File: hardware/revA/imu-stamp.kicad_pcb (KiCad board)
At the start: 4 copper layers, 19 x 7.9 mm, 37 parts, among them P1 I/O, P2 I/O, U1 LTC4317, U2 REG710NA-3.3/3K, U3 IAM-20380, U4 MMC5603NJ, U5 MC3419, U6 IAM-20380, U7 MMC5603NJ, U8 MC3419

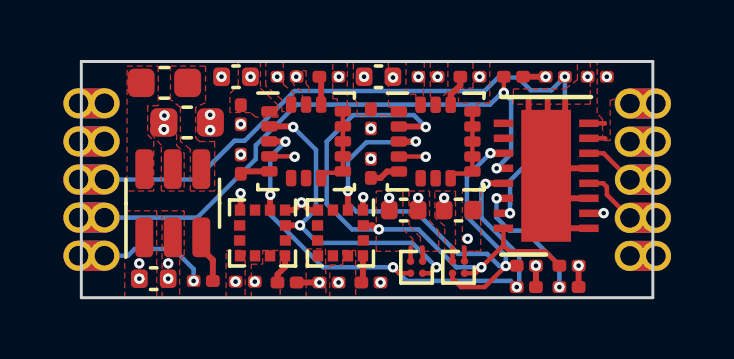
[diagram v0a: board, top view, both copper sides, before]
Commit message: updated iam20380 footprint
to exclude solder mask per AN-IVS-0002A-00
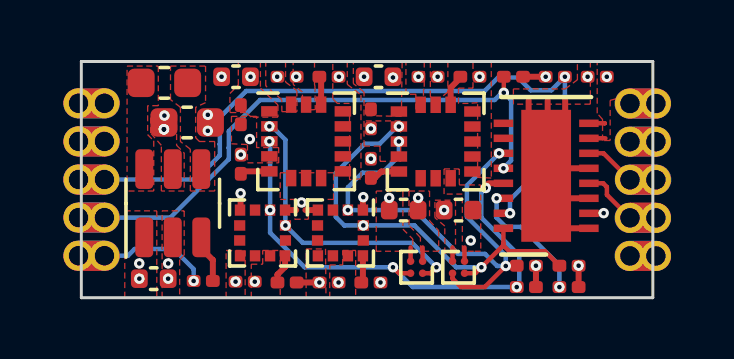
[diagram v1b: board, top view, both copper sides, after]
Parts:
- U3, U6: footprint Package_LGA:LGA-16_3x3mm_P0.5mm_LayoutBorder3x5y -> imu-stamp:IAM-20380
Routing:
- net GND: track 13.8 -> 6.31 mm, vias 22 -> 20
- net /SCL_1: track 17.9 -> 14.2 mm
- net /SDA_1: track 19.1 -> 17.0 mm
- net /SCL_0: track 20.0 -> 19.0 mm
- net /SCL: track 22.4 -> 23.2 mm

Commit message: adjusted castellated hole size and position
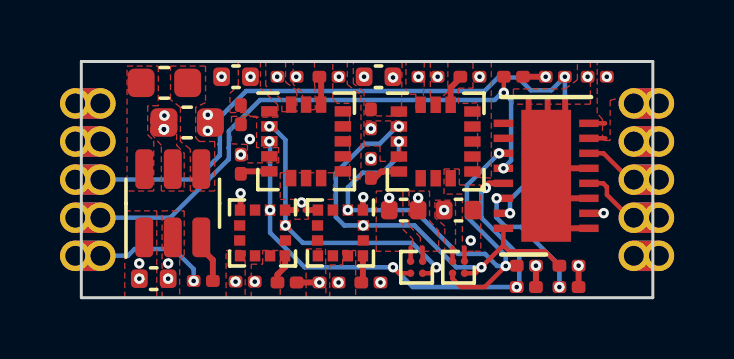
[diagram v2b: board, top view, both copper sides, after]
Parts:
- moved P1 0.14 mm to (115.3, 62.1)
- moved P2 0.13 mm to (133.1, 67.2)

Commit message: consistency updates
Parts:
- removed R1, R5: 10k, Resistor_SMD:R_0201_0603Metric
- added R2: ~, Resistor_SMD:R_0402_1005Metric, B.Cu at (130.8, 66.2)
- added R3: ~, Resistor_SMD:R_0402_1005Metric, B.Cu at (130.8, 64.6)
- added R4: ~, Resistor_SMD:R_0402_1005Metric, B.Cu at (130.8, 63.2)
- U3, U6: footprint imu-stamp:IAM-20380 -> Package_LGA:LGA-16_3x3mm_P0.5mm_LayoutBorder3x5y
- moved C1 0.69 mm to (131.2, 61.2)
- moved U1 0.33 mm to (130.4, 64.3)
- moved C8 0.32 mm to (128.0, 61.2)
- moved C7 0.13 mm to (126.4, 61.2)
- turned R15 to 90 degrees
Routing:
- net GND: track 6.31 -> 29.4 mm, vias 20 -> 22
- net 3.3V: track 5.43 -> 24.3 mm, vias 18 -> 15
- net /SCL_1: track 14.2 -> 19.7 mm
- net /XORL1: track 1.73 -> 6.02 mm
- net /SCL: track 23.2 -> 19.1 mm, vias 2 -> 1
- net /XORL2: track 2.00 -> 5.93 mm
- net Net-(U2-CP+): track 0.00 -> 2.77 mm
- net Net-(U2-CP-): track 0.00 -> 2.54 mm
- net /SCL_0: track 19.0 -> 21.0 mm
- net /SDA: track 18.8 -> 17.2 mm, vias 2 -> 1
- net VCC: track 0.00 -> 1.26 mm, vias 3 -> 2
- net /SDA_1: track 17.0 -> 16.0 mm
- net /SDA_0: track 17.8 -> 18.3 mm
- removed copper zone on F.Cu, net Net-(U2-CP+)
- removed copper zone on F.Cu, net Net-(U2-CP-)
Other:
- board text added: "3V3"
- board text added: "CH 5/23"
- board text removed: "CH 3/23"
- board text removed: "XOR_REF"

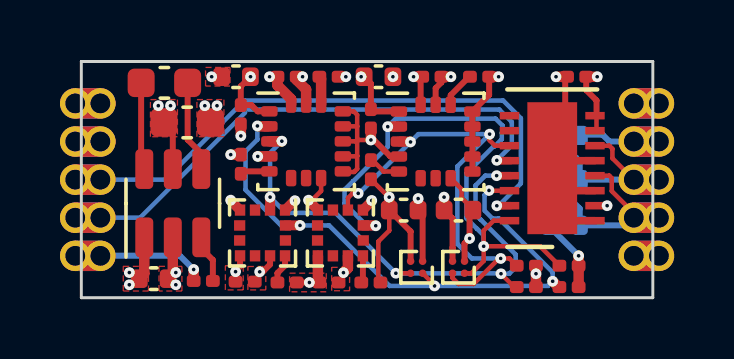
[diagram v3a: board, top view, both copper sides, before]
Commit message: resized board for manufacturing
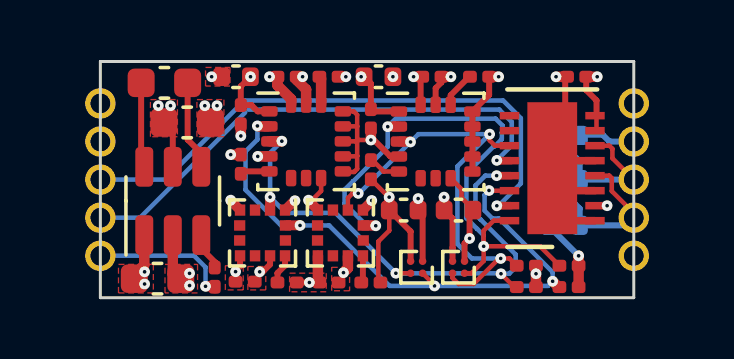
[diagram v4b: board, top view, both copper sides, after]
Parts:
- C4: footprint Capacitor_SMD:C_0402_1005Metric -> Capacitor_SMD:C_0603_1608Metric
- P1, P2: footprint imu-stamp:PinHeaderCastellated_1x05_P1.27mm_Vertical -> imu-stamp:Castellated_1x05_P1.27mm_Vertical
- R11, R12, R13, R14: value 2.7k -> 4.7k
- R2, R3, R4: value ~ -> DNP
- U1: value LTC4317 -> LTC4317I
- moved R9 0.40 mm to (119.1, 67.9), turned to 90 degrees
- moved C4 0.13 mm to (117.2, 67.9)
- moved U2 0.08 mm to (117.7, 65.4)
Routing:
- net /EN: track 3.55 -> 4.92 mm
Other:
- board size 19 x 7.9 mm -> 17.8 x 7.9 mm
- board text added: "0"
- board text added: "0 mm"
- board text added: "0.0091"
- board text added: "0.01 mm"
- board text added: "0.035 mm"
- board text added: "0.1016 mm"
- board text added: "0.11 mm"
- board text added: "0.1270 mm / 0.1270 mm"
- board text added: "0.4 mm"
- board text added: "0.7800 mm"
- board text added: "1"
- board text added: "19.0500 mm x 7.8740 mm"
- board text added: "3.3"
- board text added: "3.69"
- board text added: "4"
- board text added: "B.Cu"
- board text added: "B.Mask"
- board text added: "B.Paste"
- board text added: "B.Silkscreen"
- board text added: "BOARD CHARACTERISTICS"
- board text added: "Board Thickness:"
- board text added: "Board overall dimensions:"
- board text added: "Bottom Silk Screen"
- board text added: "Bottom Solder Mask"
- board text added: "Bottom Solder Paste"
- board text added: "Castellated pads:"
- board text added: "Color"
- board text added: "Copper Finish:"
- board text added: "Copper Layer Count:"
- board text added: "Dielectric 1"
- board text added: "Dielectric 2"
- board text added: "Dielectric 3"
- board text added: "ENIG"
- board text added: "Edge card connectors:"
- board text added: "Epsilon R"
- board text added: "F.Cu"
- board text added: "F.Mask"
- board text added: "F.Paste"
- board text added: "F.Silkscreen"
- board text added: "FR4 natural"
- board text added: "FR408-HR"
- board text added: "Impedance Control:"
- board text added: "In1.Cu"
- board text added: "In2.Cu"
- board text added: "Layer Name"
- board text added: "Loss Tangent"
- board text added: "Material"
- board text added: "Min hole diameter:"
- board text added: "Min track/spacing:"
- board text added: "No"
- board text added: "Not specified"
- board text added: "Plated Board Edge:"
- board text added: "Thickness (mm)"
- board text added: "Top Silk Screen"
- board text added: "Top Solder Mask"
- board text added: "Top Solder Paste"
- board text added: "Type"
- board text added: "Yes"
- board text added: "copper"
- board text added: "core"
- board text added: "prepreg"
